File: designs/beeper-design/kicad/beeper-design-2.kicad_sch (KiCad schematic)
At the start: 37 parts, among them U12 DRV2605YZFR, U14 EVPBB4A9B000, U15 EVPBB4A9B000, U16 EVPBB4A9B000, U4 DA7212-01UM2, U5 FH19C-6S-0.5SH(10), U6 23-23B/R6GHBHW-C30/2A, U9 LSM6DSOXTR

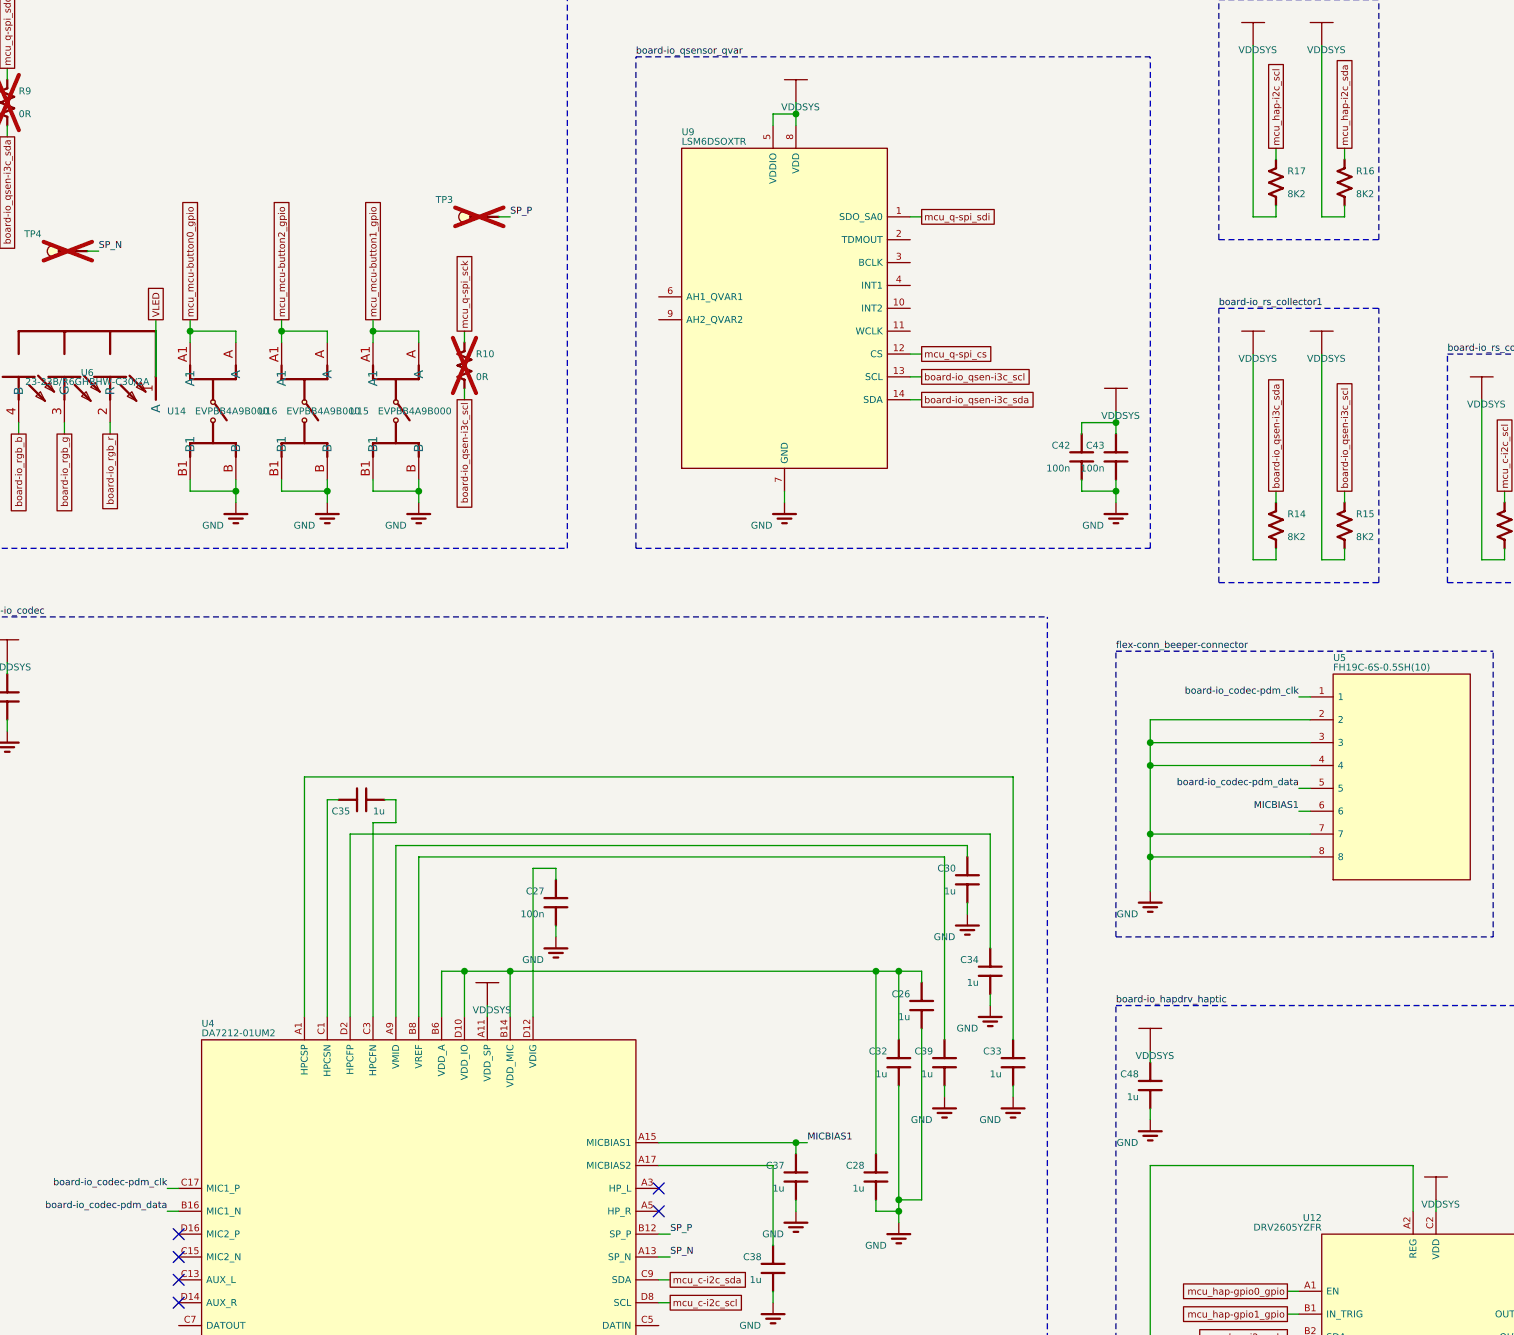
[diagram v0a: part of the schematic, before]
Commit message: better export + JLCPCB numbers
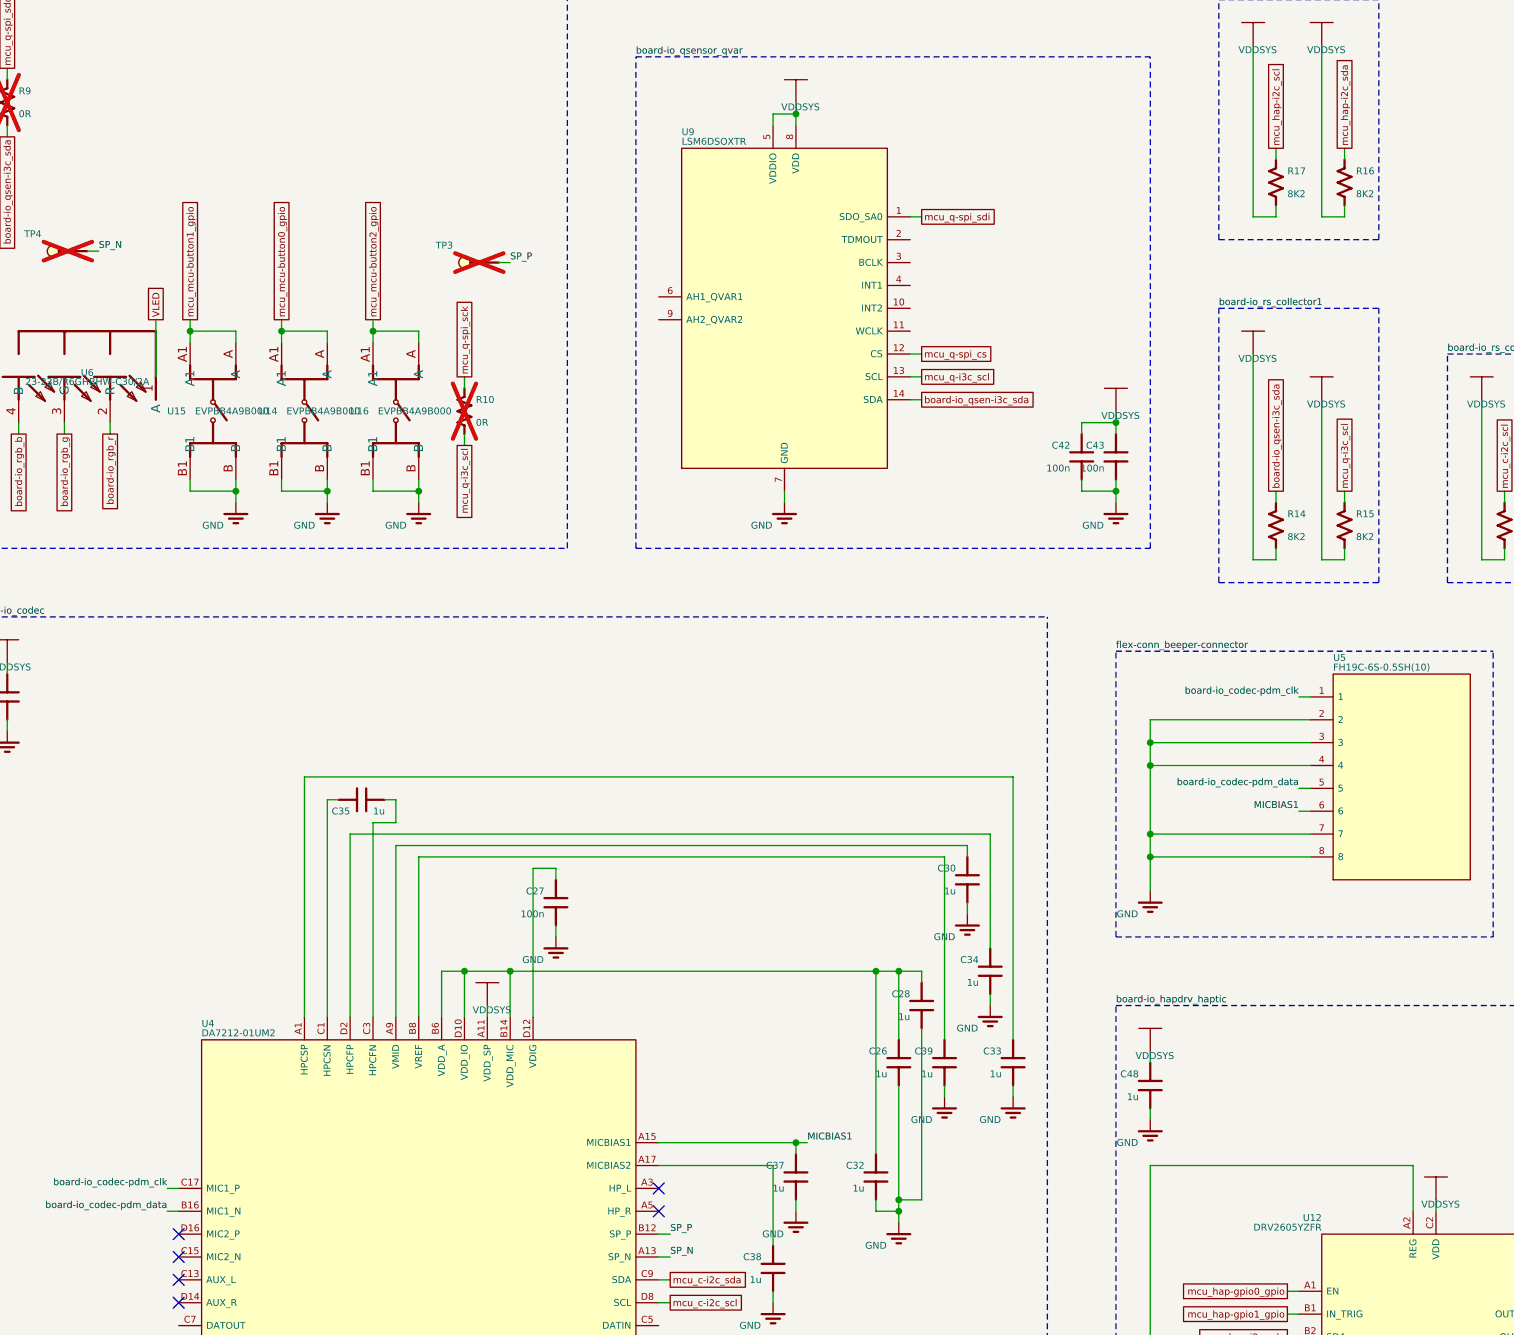
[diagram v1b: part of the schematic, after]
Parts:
- removed C26: 1u, beeper-design:Pkg0201_44, symbol C76935_14
- removed C27: 100n, beeper-design:Pkg0201_5, symbol my_capacitor
- removed C28: 1u, beeper-design:Pkg0201_17, symbol C76935_5
- removed C29: 1u, beeper-design:Pkg0201_29, symbol C76935_9
- removed C30: 1u, beeper-design:Pkg0201_15, symbol C76935_4
- removed C31: 1u, beeper-design:Pkg0201_28, symbol C76935_8
- removed C32: 1u, beeper-design:Pkg0201_40, symbol C76935_12
- removed C33: 1u, beeper-design:Pkg0201_3, symbol C76935
- removed C34: 1u, beeper-design:Pkg0201_14, symbol C76935_3
- removed C35: 1u, beeper-design:Pkg0201_38, symbol C76935_11
- removed C37: 1u, beeper-design:Pkg0201_42, symbol C76935_13
- removed C38: 1u, beeper-design:Pkg0201_4, symbol C76935_1
- removed C39: 1u, beeper-design:Pkg0201_26, symbol C76935_7
- removed C42: 100n, beeper-design:Pkg0201_45, symbol my_capacitor_9
- removed C43: 100n, beeper-design:Pkg0201_8, symbol my_capacitor_2
- removed C47: 1u, beeper-design:Pkg0201_10, symbol C76935_2
- removed C48: 1u, beeper-design:Pkg0201_22, symbol C76935_6
- added C26: 1u, beeper-design:Pkg0201_37, symbol C76935_11
- added C27: 100n, beeper-design:Pkg0201_44, symbol my_capacitor_7
- added C28: 1u, beeper-design:Pkg0201_10, symbol C76935_2
- added C29: 1u, beeper-design:Pkg0201_22, symbol C76935_6
- added C30: 1u, beeper-design:Pkg0201_8, symbol C76935_1
- added C31: 1u, beeper-design:Pkg0201_21, symbol C76935_5
- added C32: 1u, beeper-design:Pkg0201_33, symbol C76935_9
- added C33: 1u, beeper-design:Pkg0201_42, symbol C76935_12
- added C34: 1u, beeper-design:Pkg0201_7, symbol C76935
- added C35: 1u, beeper-design:Pkg0201_31, symbol C76935_8
- added C37: 1u, beeper-design:Pkg0201_35, symbol C76935_10
- added C38: 1u, beeper-design:Pkg0201_43, symbol C76935_13
- added C39: 1u, beeper-design:Pkg0201_19, symbol C76935_4
- added C42: 100n, beeper-design:Pkg0201_38, symbol my_capacitor_6
- added C43: 100n, beeper-design:Pkg0201_1, symbol my_capacitor_9
- added C47: 1u, beeper-design:Pkg0201_3, symbol C76935_14
- added C48: 1u, beeper-design:Pkg0201_15, symbol C76935_3
- R10: footprint beeper-design:Pkg0201_41 -> beeper-design:Pkg0201_34
- R12, R13: footprint beeper-design:Pkg0201_27 -> beeper-design:Pkg0201_20
- R14, R15: footprint beeper-design:Pkg0201_12 -> beeper-design:Pkg0201_5
- R16, R17: footprint beeper-design:Pkg0201_37 -> beeper-design:Pkg0201_30
- R9: footprint beeper-design:Pkg0201_32 -> beeper-design:Pkg0201_25
- U12: footprint beeper-design:LP -> beeper-design:LP_8
- U14, U15, U16: footprint beeper-design:LP_3 -> beeper-design:LP_2
- U4: footprint beeper-design:LP_4 -> beeper-design:LP_3
- U5: footprint beeper-design:LP_6 -> beeper-design:LP_5
- U6: footprint beeper-design:LP_5 -> beeper-design:LP_4
- U9: footprint beeper-design:LP_2 -> beeper-design:LP_1
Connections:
- net GND: now also C26.1, C27.1, C28.1, C29.1, C30.1, C31.1, C32.1, C33.1, C34.1, C37.1, C38.1, C39.1, C42.1, C43.1, C47.1, C48.1
- net MICBIAS1: now also C37.2
- net VDDSYS: now also C29.2, C42.2, C43.2, C48.2
- net at U4.B14 (VDD_MIC), U4.B6 (VDD_A), U4.D10 (VDD_IO): now also C26.2, C28.2, C32.2
- net at U4.A7 (DACREF): now also C31.2
- net at U4.B8 (VREF): now also C39.2
- net at U4.A17 (MICBIAS2): now also C38.2
- net at U4.D2 (HPCFP): now also C34.2
- net at U4.A9 (VMID): now also C30.2
- net at U12.A2 (REG): now also C47.2
- net at U4.C1 (HPCSN): now also C35.1
- net at U4.C3 (HPCFN): now also C35.2
- net at U4.A1 (HPCSP): now also C33.2
- net at U4.D12 (VDIG): now also C27.2
- net board-io_qsen-i3c_scl renamed mcu_q-i3c_scl

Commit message: post export, had to munge sch
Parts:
- removed C26: 1u, beeper-design:Pkg0201_37, symbol C76935_11
- removed C27: 100n, beeper-design:Pkg0201_44, symbol my_capacitor_7
- removed C28: 1u, beeper-design:Pkg0201_10, symbol C76935_2
- removed C29: 1u, beeper-design:Pkg0201_22, symbol C76935_6
- removed C30: 1u, beeper-design:Pkg0201_8, symbol C76935_1
- removed C31: 1u, beeper-design:Pkg0201_21, symbol C76935_5
- removed C32: 1u, beeper-design:Pkg0201_33, symbol C76935_9
- removed C33: 1u, beeper-design:Pkg0201_42, symbol C76935_12
- removed C34: 1u, beeper-design:Pkg0201_7, symbol C76935
- removed C35: 1u, beeper-design:Pkg0201_31, symbol C76935_8
- removed C37: 1u, beeper-design:Pkg0201_35, symbol C76935_10
- removed C38: 1u, beeper-design:Pkg0201_43, symbol C76935_13
- removed C39: 1u, beeper-design:Pkg0201_19, symbol C76935_4
- removed C42: 100n, beeper-design:Pkg0201_38, symbol my_capacitor_6
- removed C43: 100n, beeper-design:Pkg0201_1, symbol my_capacitor_9
- removed C47: 1u, beeper-design:Pkg0201_3, symbol C76935_14
- removed C48: 1u, beeper-design:Pkg0201_15, symbol C76935_3
- removed R10: 0R, beeper-design:Pkg0201_34, symbol C106228_2
- removed R12, R13: 8K2, beeper-design:Pkg0201_20, symbol my_resistor_2
- removed R16, R17: 8K2, beeper-design:Pkg0201_30, symbol my_resistor_3
- removed R9: 0R, beeper-design:Pkg0201_25, symbol C106228_1
- removed TP1, TP2: (no value), beeper-design:SMD_TESTPT, symbol smd_testpoint_cmp
- removed U12: DRV2605YZFR, beeper-design:LP_8, symbol DRV2605YZFR
- removed U5: FH19C-6S-0.5SH(10), beeper-design:LP_5, symbol FH19C_6S_0_5SH_10_
- added C26: 1u, beeper-design:Pkg0201_27, symbol C76935_8
- added C27: 100n, beeper-design:Pkg0201_38, symbol my_capacitor_13
- added C28: 1u, beeper-design:Pkg0201_5, symbol C76935_1
- added C29: 1u, beeper-design:Pkg0201_15, symbol C76935_5
- added C31: 1u, beeper-design:Pkg0201_13, symbol C76935_4
- added C32: 1u, beeper-design:Pkg0201_23, symbol C76935_6
- added C37: 1u, beeper-design:Pkg0201_26, symbol C76935_7
- added C38: 1u, beeper-design:Pkg0201_37, symbol C76935_10
- added C39: 1u, beeper-design:Pkg0201_35, symbol C76935_9
- added C42: 100n, beeper-design:Pkg0201_29, symbol my_capacitor_8
- added C43: 100n, beeper-design:Pkg0201_39, symbol my_capacitor_14
- added D1: HL-PCF-1617S39FU70GH203BC-A, beeper-design:LP_5, symbol C513368
- added R10: 0R, beeper-design:Pkg0201_28, symbol my_resistor_8
- added R12, R13: 8K2, beeper-design:Pkg0201_17, symbol my_resistor_4
- added TP3: (no value), beeper-design:SMD_TESTPT, symbol smd_testpoint_cmp
- C30: renamed from U6; value 23-23B/R6GHBHW-C30/2A -> 1u; footprint beeper-design:LP_4 -> beeper-design:Pkg0201_3; symbol L23_23B_R6GHBHW_C30_2A -> C76935; MPN 23-23B/R6GHBHW-C30/2A -> GRM033R61A105ME44D; Manufacturer Everlight -> MURATA; Name board-io_led -> board-io_codec_cap; Reference-prefix (none) -> C
- R14, R15: footprint beeper-design:Pkg0201_5 -> beeper-design:Pkg0201_1; MPN RC0201DR-078K2L -> RMCF0201JT8K20; Manufacturer YAGEO -> Stackpole Electronics Inc
- R9: renamed from TP3; value (none) -> 0R; footprint beeper-design:SMD_TESTPT -> beeper-design:Pkg0201_19; symbol smd_testpoint_cmp -> my_resistor_5; MPN (none) -> CR0201-J/-000GLF; Manufacturer (none) -> BOURNS; Name board-io_sp-pin0 -> board-io_rs-sda; Reference-prefix TP -> R
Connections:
- net GND: now also C30.1, C26.1, C27.1, C28.1, C29.1, C31.1, C32.1, C37.1, C38.1, C39.1, C42.1, C43.1
- net MICBIAS1: now also C37.2
- net SP_P: now also TP3.p; no longer R9.p
- net VLED: now also D1.2; no longer C30.1 (A)
- net board-io_qsen-i3c_sda: now also R9.1
- net board-io_rgb_b: now also D1.4; no longer C30.4 (B)
- net board-io_rgb_g: now also D1.3; no longer C30.3 (G)
- net board-io_rgb_r: now also D1.1; no longer C30.2 (R)
- net mcu_q-spi_sck: now also R10.2
- net mcu_q-spi_sdo: now also R9.2
- net at U4.A9 (VMID): now also C30.2
- net at U4.A17 (MICBIAS2): now also C38.2
- net at U4.A7 (DACREF): now also C31.2
- net at U4.B14 (VDD_MIC), U4.B6 (VDD_A), U4.D10 (VDD_IO): now also C26.2, C28.2, C32.2
- net at U4.B8 (VREF): now also C39.2
- net at U4.D12 (VDIG): now also C27.2
- net VDDSYS renamed VDD1P8
- net VDD1P8: now also C29.2, C42.2, C43.2, R12.2, R13.2
- net board-io_codec-pdm_clk renamed codec-pdm-net_clk
- net board-io_codec-pdm_data renamed codec-pdm-net_data
- net mcu_c-i2c_scl renamed codec-i2c-net_scl
- net codec-i2c-net_scl: now also R13.1
- net mcu_c-i2c_sda renamed codec-i2c-net_sda
- net codec-i2c-net_sda: now also R12.1
- net mcu_q-i3c_scl renamed board-io_qsen-i3c_scl
- net board-io_qsen-i3c_scl: now also R10.1
